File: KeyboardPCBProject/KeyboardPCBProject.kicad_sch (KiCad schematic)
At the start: 0 parts

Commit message: Added some resistors
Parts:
- added R1: R_Small, symbol Device:R_Small
- added R? (x2): 22, symbol Device:R_Small
- added U1: ATmega32U4-A, Package_QFP:TQFP-44_10x10mm_P0.8mm, symbol MCU_Microchip_ATmega:ATmega32U4-A
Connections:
- new net: R1.1, U1.33 (~{HWB}/PE2)
- new net: R?.2, U1.4 (D+)
- new net: R?.2, U1.3 (D-)
- new net +5V: U1.14 (VCC), U1.2 (UVCC), U1.24 (AVCC), U1.34 (VCC), U1.44 (AVCC)
- new net GND: R1.2, U1.15 (GND), U1.23 (GND), U1.35 (GND), U1.43 (GND), U1.5 (UGND)

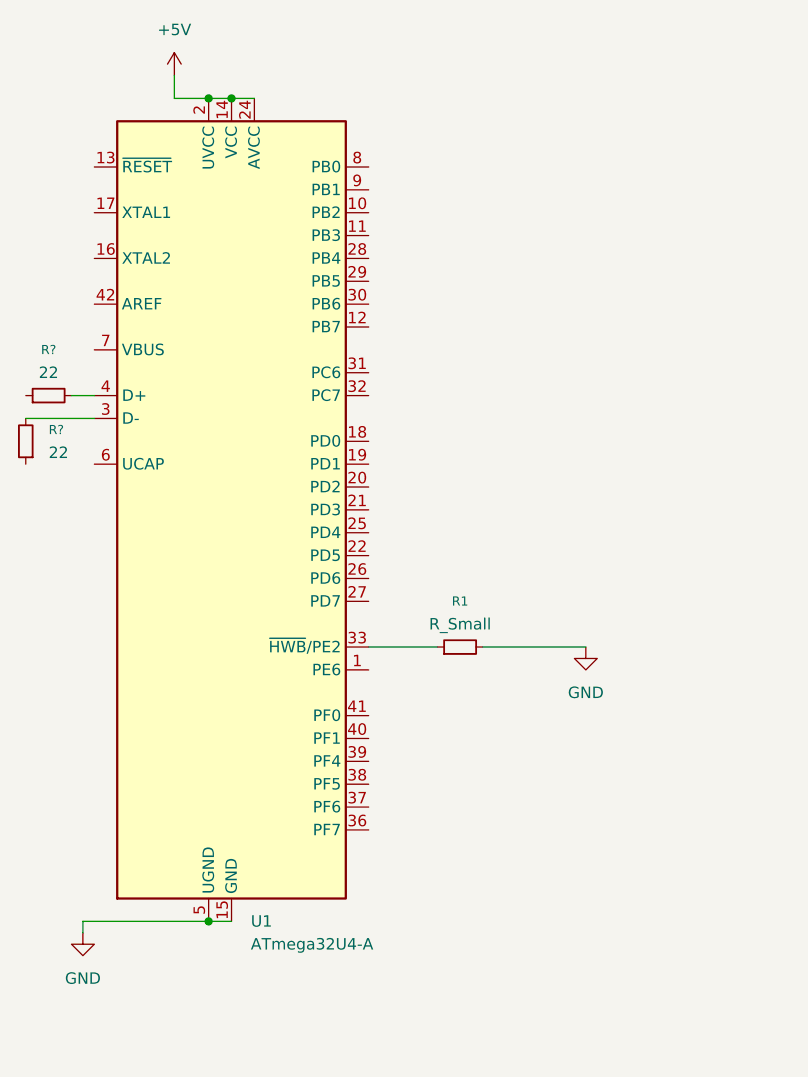
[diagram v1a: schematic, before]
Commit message: Added Capactiors and Resistors
I cant spell
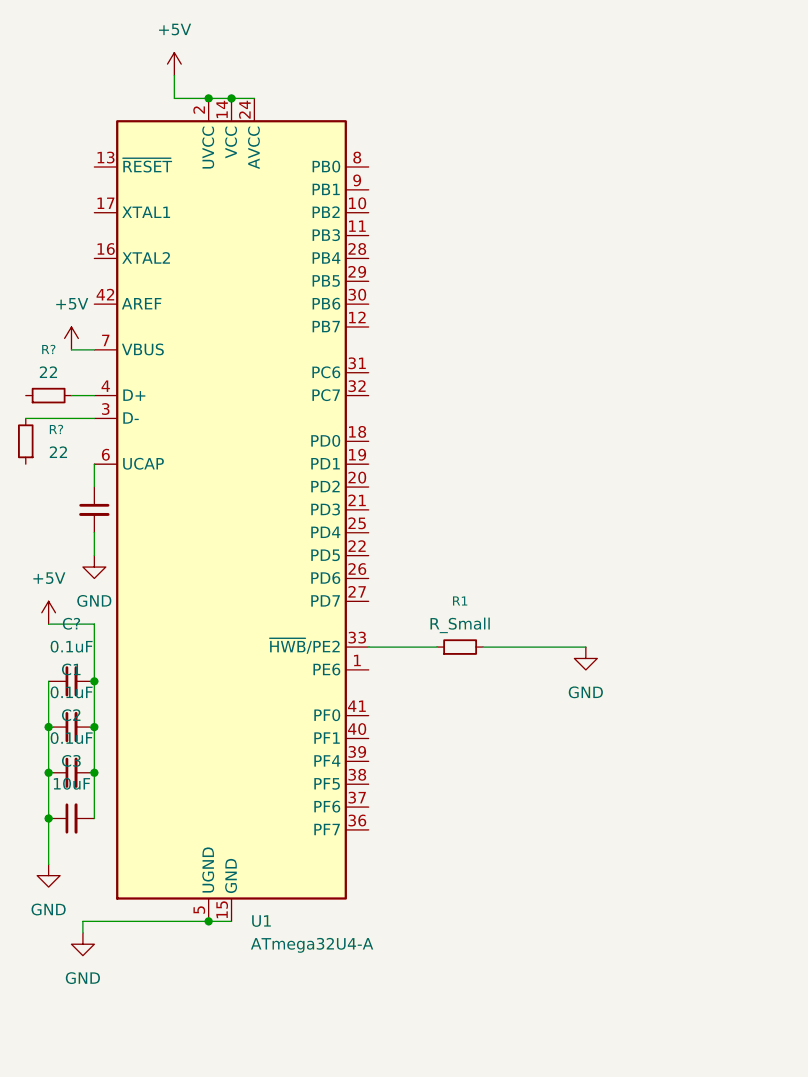
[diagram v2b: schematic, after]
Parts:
- added C1, C2, C?: 0.1uF, symbol Device:C_Small
- added C3: 10uF, symbol Device:C_Small
- added C?: 1uF, symbol Device:C_Small
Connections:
- net +5V: now also U1.7 (VBUS), C1.2, C2.2, C3.2, C?.2
- net GND: now also C1.1, C2.1, C3.1, C?.1, C?.2
- net at U1.6 (UCAP): now also C?.1

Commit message: Finished Step 3
If there are any issues its %100 with Crystal-gmu24 cause its a 4 pin connector only showing 3 pins. Gemini told me it should be fine and that its just a better display of what it looks like but I don't know.
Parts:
- added C4, C?: 22pF, symbol Device:C_Small
- added R?: 10k, symbol Device:R_Small
- added SW1: SW_Push, symbol Switch:SW_Push
- added Y1: Crystal_GND24_Small, symbol Device:Crystal_GND24_Small
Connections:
- net +5V: now also R?.1; no longer U1.7 (VBUS)
- net GND: now also C4.2, C?.1, SW1.1, Y1.2 (G), Y1.4 (G)
- net D +: now reaches R?.1
- net D -: now reaches R?.2, U1.3 (D-)
- net at U1.13 (~{RESET}): now also R?.2, SW1.2
- net at U1.16 (XTAL2): now also C?.2, Y1.3
- net at U1.17 (XTAL1): now also C4.1, Y1.1
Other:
- moved on the sheet: C1, C2, C3, C?, R1, R?, U1
